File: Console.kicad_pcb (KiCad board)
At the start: 2 copper layers, 64 x 64 mm, 62 parts, among them J1 batt_in, J11 lcd_out, J14 gnd_out, J17 node_conn_1, J18 node_conn_2, J2 3v3_gnd, J3 motor_out, J4 ir_out, J5 pwr_jumper, J6 gpio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

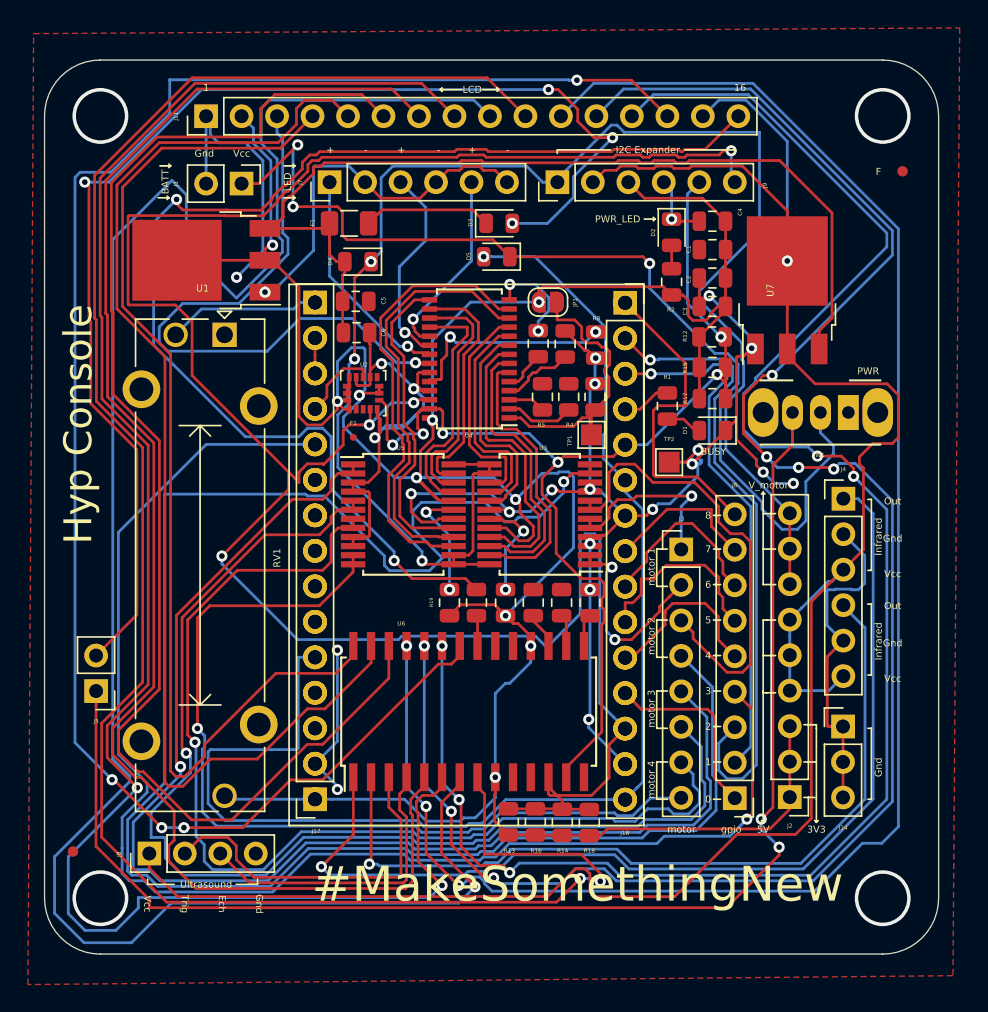
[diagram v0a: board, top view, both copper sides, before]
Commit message: Change NodeMCU Vin
Update the nodeMcu supply voltage to 5v from 3v3
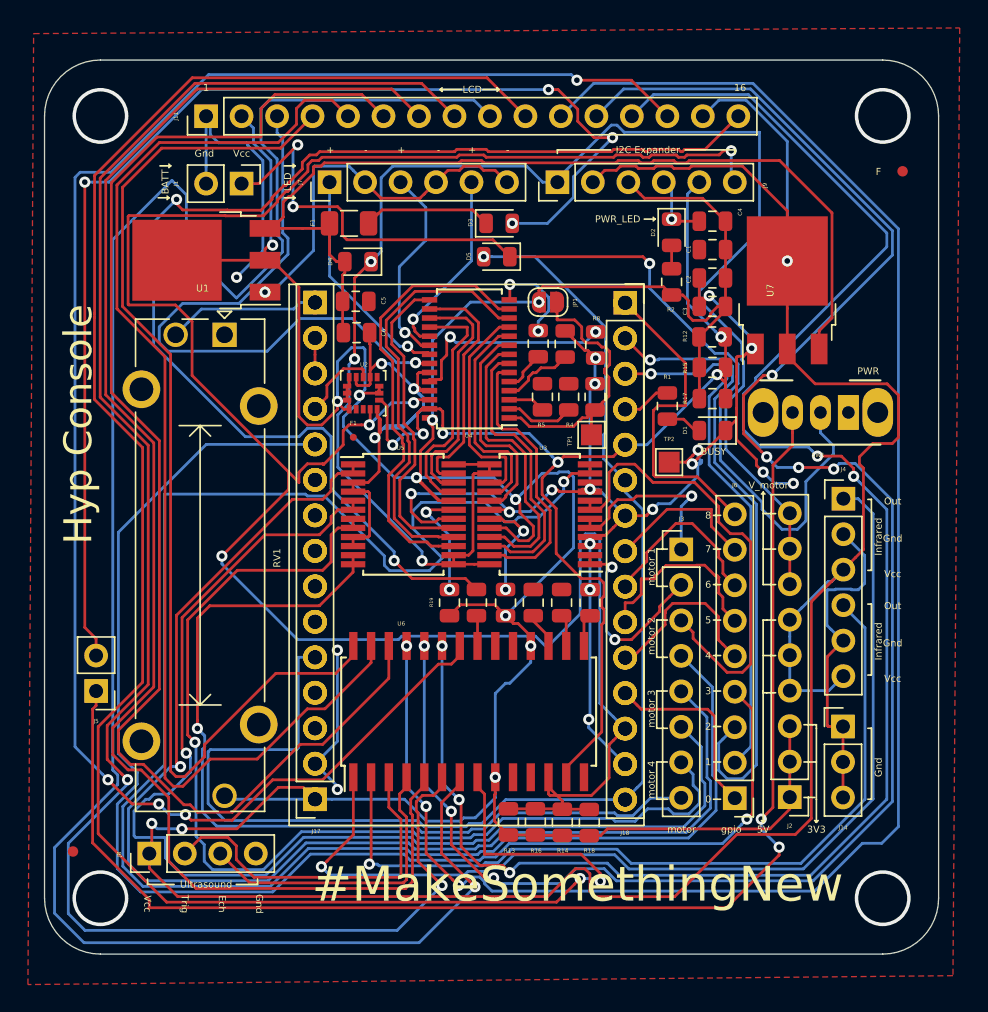
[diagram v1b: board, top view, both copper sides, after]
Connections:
- J17 pad 1: +3V3 -> +5V
- NMCU1 pad VIN: +3V3 -> +5V
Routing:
- net +5V: track 154.4 -> 170.1 mm, vias 1 -> 3
- net /SWITCH_OUT: track 89.7 -> 87.3 mm
- net /m32: track 83.9 -> 86.3 mm
- net /LCD_D7: track 124.1 -> 122.7 mm
- net /LCD_D1: track 126.1 -> 125.1 mm
- net /LCD_D2: track 142.0 -> 141.2 mm
- net /m31: track 91.0 -> 91.7 mm
